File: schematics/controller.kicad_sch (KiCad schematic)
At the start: 21 parts, among them U6 ESP32-S3-WROOM-1-N8R8, U8 PCA9685PW_118

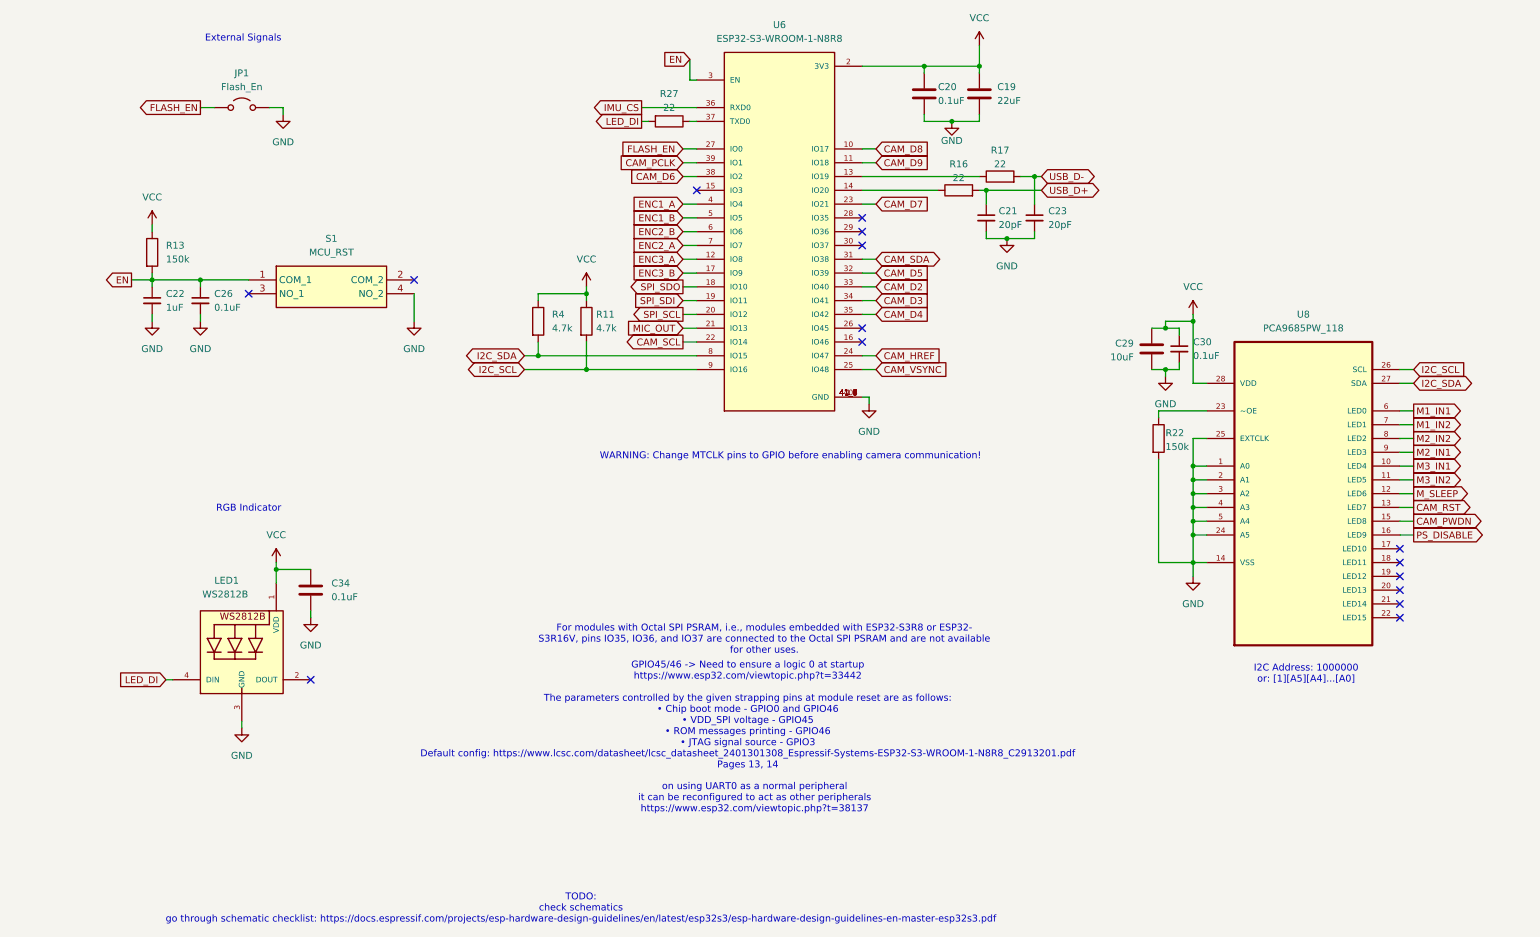
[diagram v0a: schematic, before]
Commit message: Fixed mistake in battery bypass circuit.
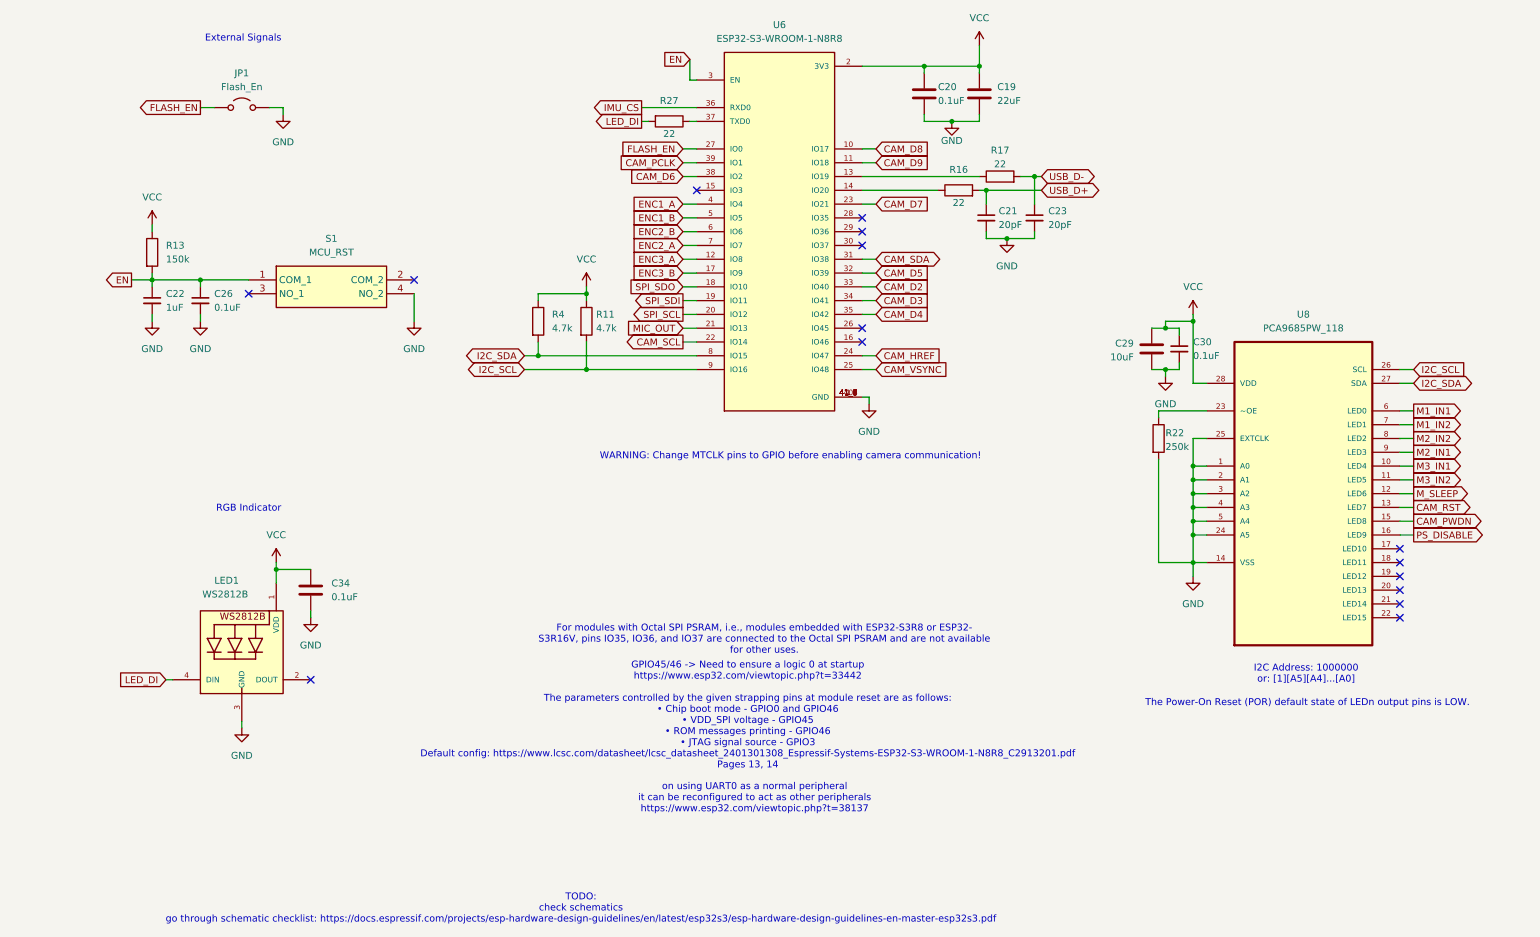
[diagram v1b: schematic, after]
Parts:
- R22: value 150k -> 250k
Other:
- note added: "The Power-On Reset (POR) default state of LEDn output pins is LOW."
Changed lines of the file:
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@@
 		)
 	)
+	(text "The Power-On Reset (POR) default state of LEDn output pins is LOW."
+		(exclude_from_sim no)
+		(at 240.792 147.828 0)
+		(effects
+			(font
+				(size 1.27 1.27)
+			)
+		)
+	)
 	(text "RGB Indicator"
 		(exclude_from_sim no)
@@
 	)
 	(global_label "SPI_SDO"
-		(shape output)
+		(shape input)
 		(at 125.73 71.12 180)
 		(fields_autoplaced yes)
@@
 	)
 	(global_label "SPI_SDI"
-		(shape input)
+		(shape output)
 		(at 125.73 73.66 180)
 		(fields_autoplaced yes)
@@
 			)
 		)
-		(property "Value" "150k"
+		(property "Value" "250k"
 			(at 214.63 100.584 0)
 			(effects
@@
 		(dnp no)
 		(property "Reference" "R27"
-			(at 123.19 35.56 90)
+			(at 123.19 36.83 90)
 			(effects
 				(font
@@
 		)
 		(property "Value" "22"
-			(at 123.19 38.1 90)
+			(at 123.19 42.926 90)
 			(effects
 				(font
@@
 		(dnp no)
 		(property "Reference" "R16"
-			(at 176.53 48.514 90)
+			(at 176.53 49.53 90)
 			(effects
 				(font
@@
 		)
 		(property "Value" "22"
-			(at 176.53 51.054 90)
+			(at 176.53 55.626 90)
 			(effects
 				(font

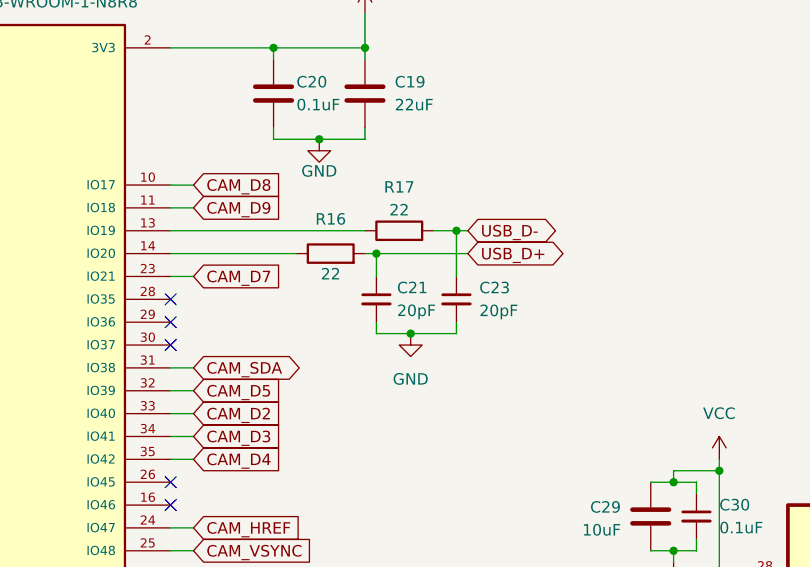
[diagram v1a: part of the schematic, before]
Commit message: Rerouted part of the board containing 3.3v regulator and USB connectivity. Routed 90ohm diff pair controlled-impedance traces for USB 2.0 Full Speed.
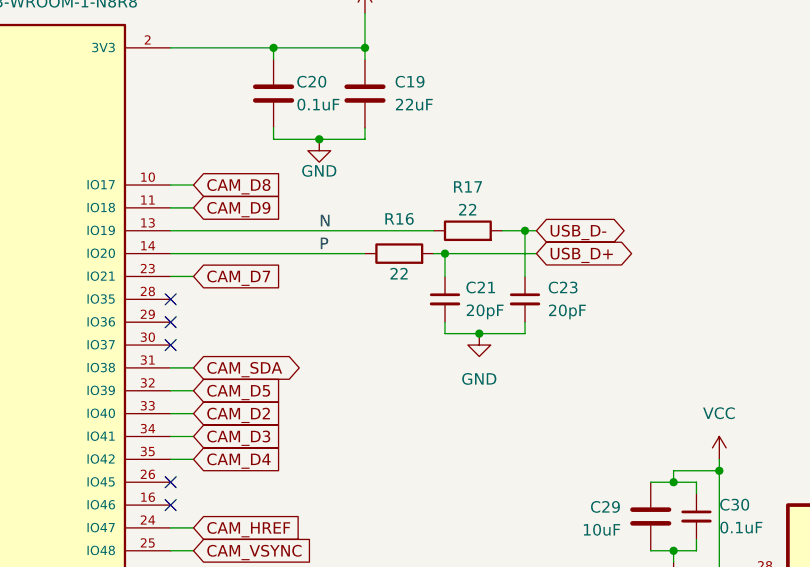
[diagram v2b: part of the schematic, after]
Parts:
- R16, R17: footprint Resistor_SMD:R_0603_1608Metric_Pad0.98x0.95mm_HandSolder -> Resistor_SMD:R_0402_1005Metric_Pad0.72x0.64mm_HandSolder
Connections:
- net N: now reaches R17.1, U6.13 (IO19)
- net P: now reaches R16.1, U6.14 (IO20)
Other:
- moved on the sheet: C21, C23, R16, R17
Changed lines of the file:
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@@
 	)
 	(junction
-		(at 185.42 62.23)
+		(at 193.04 62.23)
 		(diameter 0)
 		(color 0 0 0 0)
 	)
 	(junction
-		(at 181.61 53.34)
+		(at 189.23 53.34)
 		(diameter 0)
 		(color 0 0 0 0)
@@
 	)
 	(junction
-		(at 190.5 50.8)
+		(at 198.12 50.8)
 		(diameter 0)
 		(color 0 0 0 0)
@@
 	(wire
 		(pts
-			(xy 190.5 62.23) (xy 185.42 62.23)
+			(xy 198.12 62.23) (xy 193.04 62.23)
 		)
 		(stroke
@@
 	(wire
 		(pts
-			(xy 181.61 53.34) (xy 181.61 55.88)
+			(xy 189.23 53.34) (xy 189.23 55.88)
 		)
 		(stroke
@@
 	(wire
 		(pts
-			(xy 181.61 60.96) (xy 181.61 62.23)
+			(xy 189.23 60.96) (xy 189.23 62.23)
 		)
 		(stroke
@@
 	(wire
 		(pts
-			(xy 181.61 62.23) (xy 185.42 62.23)
+			(xy 189.23 62.23) (xy 193.04 62.23)
 		)
 		(stroke
@@
 	(wire
 		(pts
-			(xy 190.5 50.8) (xy 190.5 55.88)
+			(xy 198.12 50.8) (xy 198.12 55.88)
 		)
 		(stroke
@@
 	(wire
 		(pts
-			(xy 158.75 50.8) (xy 180.34 50.8)
+			(xy 158.75 50.8) (xy 187.96 50.8)
 		)
 		(stroke
@@
 	(wire
 		(pts
-			(xy 180.34 53.34) (xy 181.61 53.34)
+			(xy 187.96 53.34) (xy 189.23 53.34)
 		)
 		(stroke
@@
 	(wire
 		(pts
-			(xy 158.75 53.34) (xy 172.72 53.34)
+			(xy 158.75 53.34) (xy 180.34 53.34)
 		)
 		(stroke
@@
 	(wire
 		(pts
-			(xy 187.96 50.8) (xy 190.5 50.8)
+			(xy 195.58 50.8) (xy 198.12 50.8)
 		)
 		(stroke
@@
 	(wire
 		(pts
-			(xy 190.5 60.96) (xy 190.5 62.23)
+			(xy 198.12 60.96) (xy 198.12 62.23)
 		)
 		(stroke
@@
 	(wire
 		(pts
-			(xy 190.5 50.8) (xy 191.77 50.8)
+			(xy 198.12 50.8) (xy 199.39 50.8)
 		)
 		(stroke
@@
 	(wire
 		(pts
-			(xy 181.61 53.34) (xy 191.77 53.34)
+			(xy 189.23 53.34) (xy 199.39 53.34)
 		)
 		(stroke
@@
 		)
 	)
+	(label "N"
+		(at 175.26 50.8 0)
+		(fields_autoplaced yes)
+		(effects
+			(font
+				(size 1.27 1.27)
+			)
+			(justify left bottom)
+		)
+	)
+	(label "P"
+		(at 175.26 53.34 0)
+		(fields_autoplaced yes)
+		(effects
+			(font
+				(size 1.27 1.27)
+			)
+			(justify left bottom)
+		)
+	)
 	(global_label "M3_IN2"
 		(shape output)
@@
 	(global_label "USB_D-"
 		(shape bidirectional)
-		(at 191.77 50.8 0)
+		(at 199.39 50.8 0)
 		(fields_autoplaced yes)
 		(effects
@@
 		)
 		(property "Intersheetrefs" "${INTERSHEET_REFS}"
-			(at 203.4865 50.8 0)
+			(at 211.1065 50.8 0)
 			(effects
 				(font
@@
 	(global_label "USB_D+"
 		(shape bidirectional)
-		(at 191.77 53.34 0)
+		(at 199.39 53.34 0)
 		(fields_autoplaced yes)
 		(effects
@@
 		)
 		(property "Intersheetrefs" "${INTERSHEET_REFS}"
-			(at 203.4865 53.34 0)
+			(at 211.1065 53.34 0)
 			(effects
 				(font
@@
 	(symbol
 		(lib_id "Device:R")
-		(at 184.15 50.8 90)
+		(at 191.77 50.8 90)
 		(unit 1)
 		(exclude_from_sim no)
@@
 		(dnp no)
 		(property "Reference" "R17"
-			(at 184.15 45.974 90)
+			(at 191.77 45.974 90)
 			(effects
 				(font
@@
 		)
 		(property "Value" "22"
-			(at 184.15 48.514 90)
+			(at 191.77 48.514 90)
 			(effects
 				(font
@@
 			)
 		)
-		(property "Footprint" "Resistor_SMD:R_0603_1608Metric_Pad0.98x0.95mm_HandSolder"
-			(at 184.15 52.578 90)
+		(property "Footprint" "Resistor_SMD:R_0402_1005Metric_Pad0.72x0.64mm_HandSolder"
+			(at 191.77 52.578 90)
 			(effects
 				(font
@@
 		)
 		(property "Datasheet" "~"
-			(at 184.15 50.8 0)
+			(at 191.77 50.8 0)
 			(effects
 				(font
@@
 		)
 		(property "Description" "Resistor"
-			(at 184.15 50.8 0)
+			(at 191.77 50.8 0)
 			(effects
 				(font
@@
 	(symbol
 		(lib_id "power:GND")
-		(at 185.42 62.23 0)
+		(at 193.04 62.23 0)
 		(unit 1)
 		(exclude_from_sim no)
@@
 		(fields_autoplaced yes)
 		(property "Reference" "#PWR059"
-			(at 185.42 68.58 0)
+			(at 193.04 68.58 0)
 			(effects
 				(font
@@
 		)
 		(property "Value" "GND"
-			(at 185.42 67.31 0)
+			(at 193.04 67.31 0)
 			(effects
 				(font
@@
 		)
 		(property "Footprint" ""
-			(at 185.42 62.23 0)
+			(at 193.04 62.23 0)
 			(effects
 				(font
@@
 		)
 		(property "Datasheet" ""
-			(at 185.42 62.23 0)
+			(at 193.04 62.23 0)
 			(effects
 				(font
@@
 		)
 		(property "Description" "Power symbol creates a global label with name \"GND\" , ground"
-			(at 185.42 62.23 0)
+			(at 193.04 62.23 0)
 			(effects
 				(font
@@
 	(symbol
 		(lib_id "Device:C_Small")
-		(at 190.5 58.42 0)
+		(at 198.12 58.42 0)
 		(unit 1)
 		(exclude_from_sim no)
@@
 		(fields_autoplaced yes)
 		(property "Reference" "C23"
-			(at 193.04 57.1562 0)
+			(at 200.66 57.1562 0)
 			(effects
 				(font
@@
 		)
 		(property "Value" "20pF"
-			(at 193.04 59.6962 0)
+			(at 200.66 59.6962 0)
 			(effects
 				(font
@@
 		)
 		(property "Footprint" "Capacitor_SMD:C_0402_1005Metric_Pad0.74x0.62mm_HandSolder"
-			(at 190.5 58.42 0)
+			(at 198.12 58.42 0)
 			(effects
 				(font
@@
 		)
 		(property "Datasheet" "~"
-			(at 190.5 58.42 0)
+			(at 198.12 58.42 0)
 			(effects
 				(font
@@
 		)
 		(property "Description" "Unpolarized capacitor, small symbol"
-			(at 190.5 58.42 0)
+			(at 198.12 58.42 0)
 			(effects
 				(font
@@
 	(symbol
 		(lib_id "Device:C_Small")
-		(at 181.61 58.42 0)
+		(at 189.23 58.42 0)
 		(unit 1)
 		(exclude_from_sim no)
@@
 		(dnp no)
 		(property "Reference" "C21"
-			(at 183.896 57.15 0)
+			(at 191.516 57.15 0)
 			(effects
 				(font
@@
 		)
 		(property "Value" "20pF"
-			(at 183.896 59.69 0)
+			(at 191.516 59.69 0)
 			(effects
 				(font
@@
 		)
 		(property "Footprint" "Capacitor_SMD:C_0402_1005Metric_Pad0.74x0.62mm_HandSolder"
-			(at 181.61 58.42 0)
+			(at 189.23 58.42 0)
 			(effects
 				(font
@@
 		)
 		(property "Datasheet" "~"
-			(at 181.61 58.42 0)
+			(at 189.23 58.42 0)
 			(effects
 				(font
@@
 		)
 		(property "Description" "Unpolarized capacitor, small symbol"
-			(at 181.61 58.42 0)
+			(at 189.23 58.42 0)
 			(effects
 				(font
@@
 	(symbol
 		(lib_id "Device:R")
-		(at 176.53 53.34 90)
+		(at 184.15 53.34 90)
 		(unit 1)
 		(exclude_from_sim no)
@@
 		(dnp no)
 		(property "Reference" "R16"
-			(at 176.53 49.53 90)
+			(at 184.15 49.53 90)
 			(effects
 				(font
@@
 		)
 		(property "Value" "22"
-			(at 176.53 55.626 90)
+			(at 184.15 55.626 90)
 			(effects
 				(font
@@
 			)
 		)
-		(property "Footprint" "Resistor_SMD:R_0603_1608Metric_Pad0.98x0.95mm_HandSolder"
-			(at 176.53 55.118 90)
+		(property "Footprint" "Resistor_SMD:R_0402_1005Metric_Pad0.72x0.64mm_HandSolder"
+			(at 184.15 55.118 90)
 			(effects
 				(font
@@
 		)
 		(property "Datasheet" "~"
-			(at 176.53 53.34 0)
+			(at 184.15 53.34 0)
 			(effects
 				(font
@@
 		)
 		(property "Description" "Resistor"
-			(at 176.53 53.34 0)
+			(at 184.15 53.34 0)
 			(effects
 				(font
